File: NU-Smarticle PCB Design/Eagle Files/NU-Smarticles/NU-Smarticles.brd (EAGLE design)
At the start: 20 x 48 mm, 66 parts, among them IC1 CP2104, IC2 ATMEGA328P, Q3 DMG341, SW2 KMR2, U6 AP2112-3.3, U7 MCP73831T-2ACI/OT, U8 OPA344, U9 ADMP401, X1 JSTPH, X4 20329, Y2 CSTCE16M0V53-R0 8MHZ

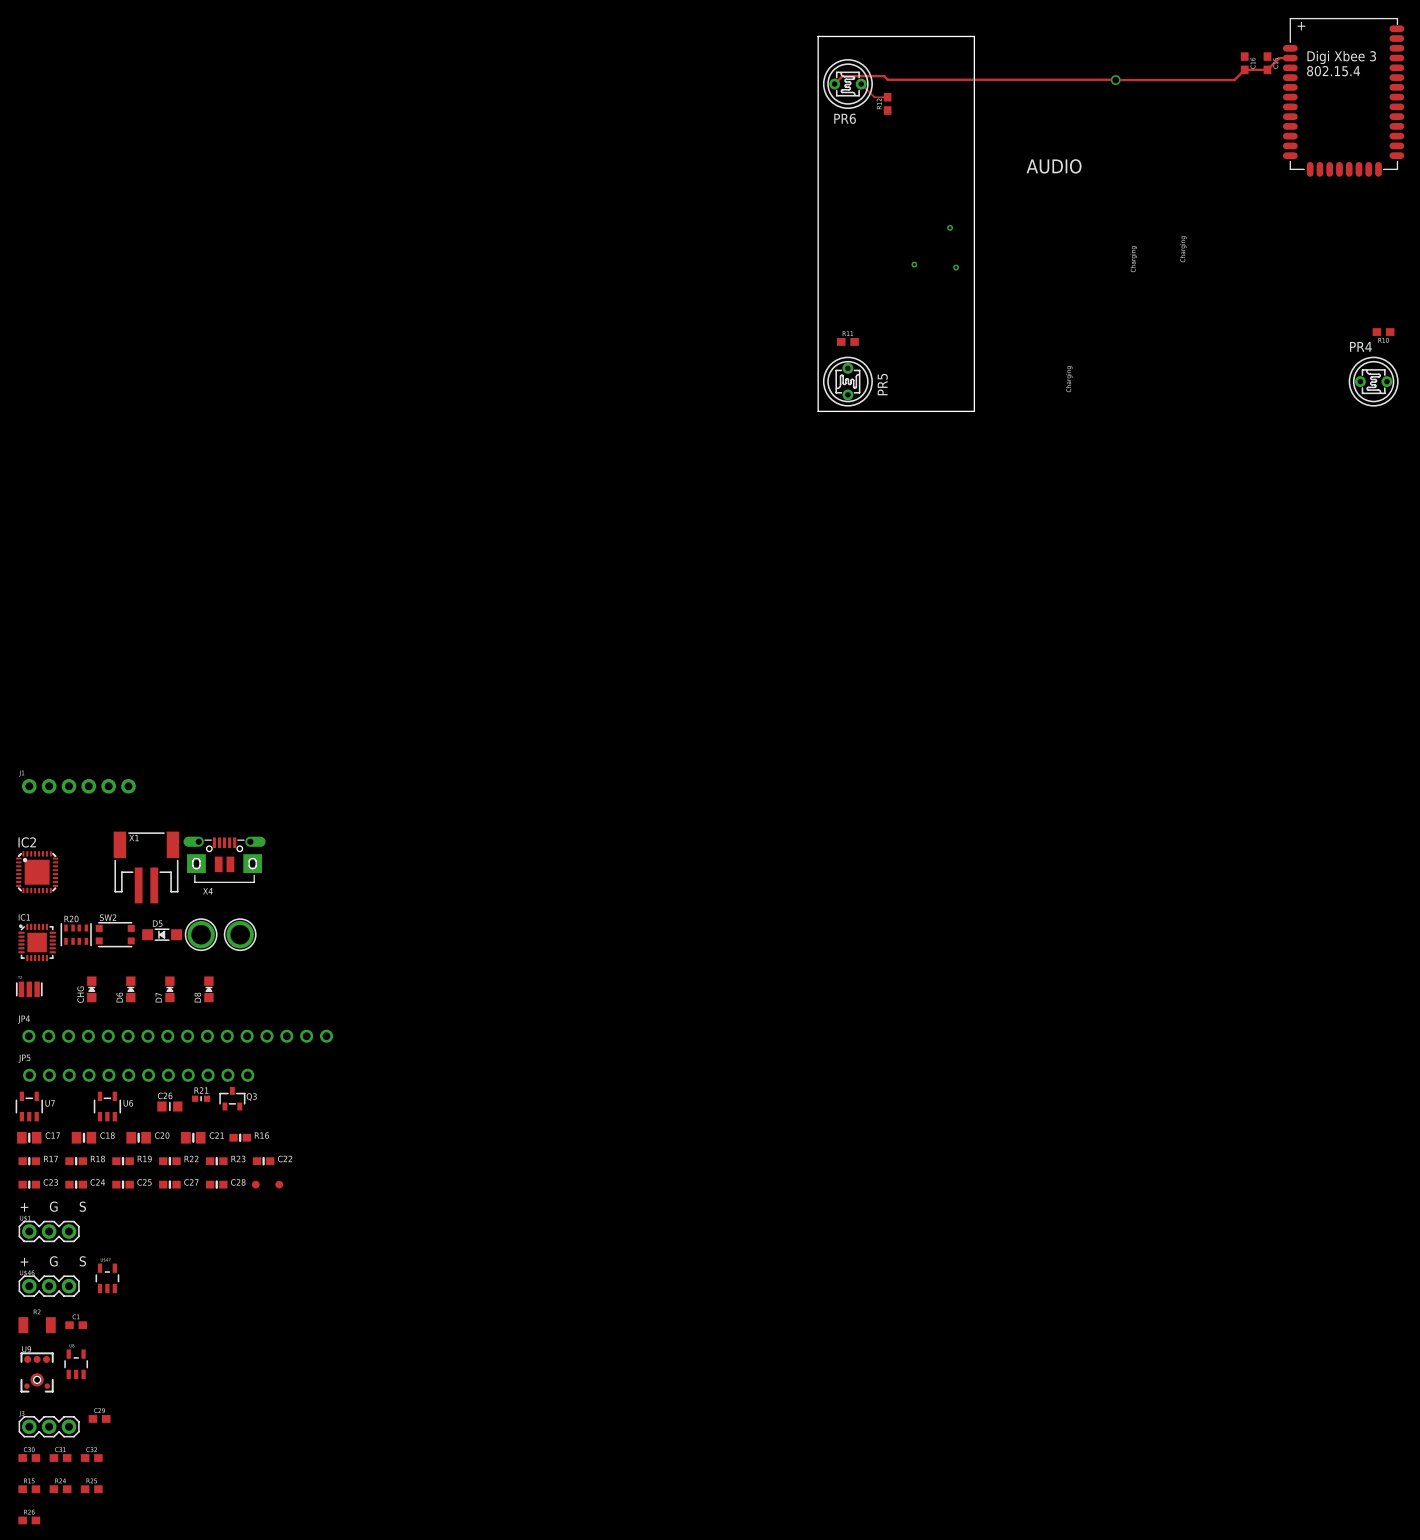
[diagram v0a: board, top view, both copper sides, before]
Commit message: include v2 Smarticles
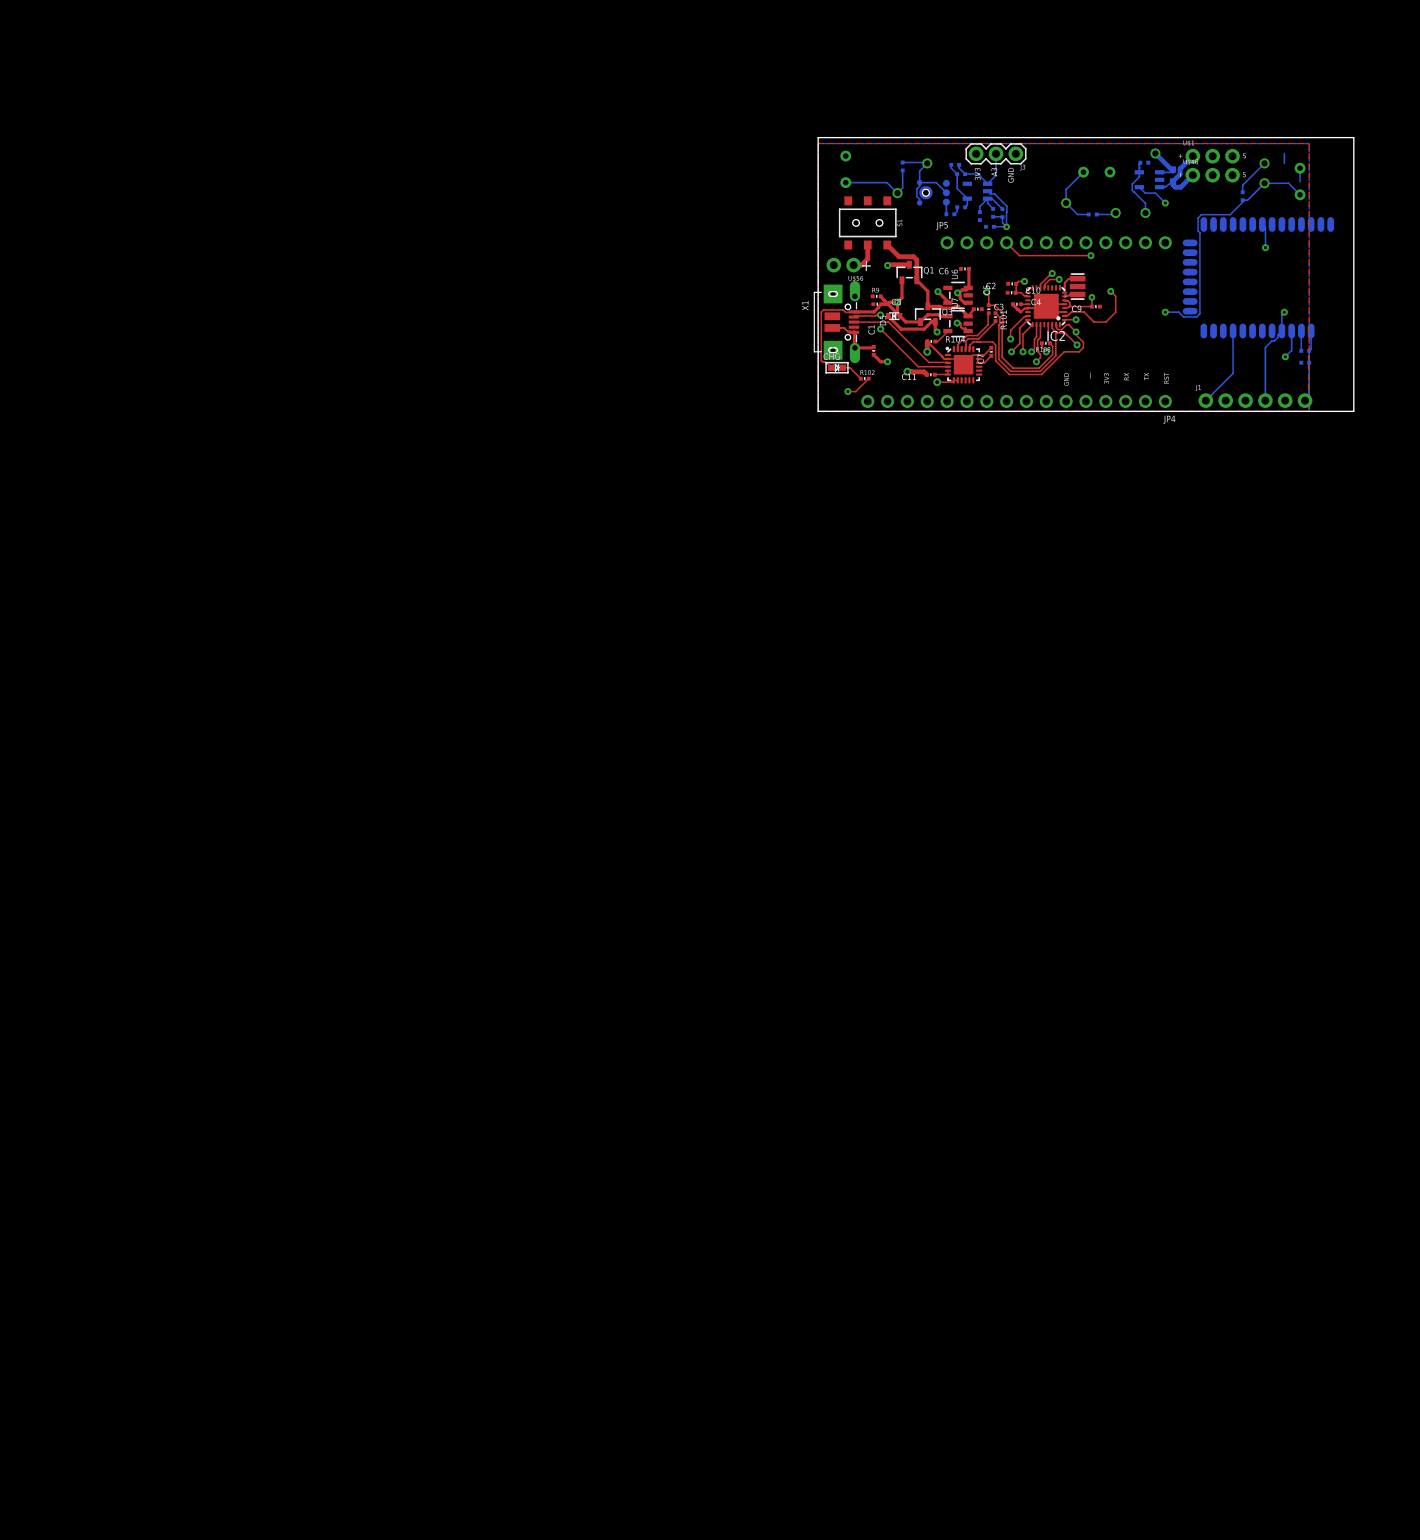
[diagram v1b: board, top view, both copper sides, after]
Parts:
- removed C20, C21: 10uF, microbuilder:0805-NO
- removed C22, C23, C24, C25: 0.1uF, microbuilder:0603-NO
- removed C26: 10uF, microbuilder:_0805MP
- removed C27, C28: 1uF, microbuilder:0603-NO
- removed C29: 100pF, SparkFun-Capacitors:0603
- removed C30: 4.7uF, SparkFun-Capacitors:0603
- removed C31: 1.0uF, SparkFun-Capacitors:0603
- removed C32: 0.1uF, SparkFun-Capacitors:0603
- removed D6: RED, microbuilder:CHIPLED_0805_NOOUTLINE
- removed D7, D8: YELLOW, microbuilder:CHIPLED_0805_NOOUTLINE
- removed FRAME1: FRAME-LETTER, SparkFun-Aesthetics:CREATIVE_COMMONS
- removed PR4, PR5, PR6: A1050_09, photo-elements:T0-46-A10XX
- removed R10, R11, R12, R15, R24: 10k, SparkFun-Resistors:0603
- removed R16, R17, R22, R23: 1K, microbuilder:0603-NO
- removed R18, R19: 10K, microbuilder:0603-NO
- removed R20: 100K, microbuilder:RESPACK_4X0603
- removed R21: 1K, microbuilder:_0603MP
- removed R25: 1.5k, SparkFun-Resistors:0603
- removed R26: 100k, SparkFun-Resistors:0603
- removed SW2: KMR2, microbuilder:BTN_KMR2_4.6X2.8
- removed U$31, U$32: MOUNTINGHOLE2.5, microbuilder:MOUNTINGHOLE_2.5_PLATED
- removed U$34, U$35: FIDUCIAL_1MM, microbuilder:FIDUCIAL_1MM
- removed X4: 20329, microbuilder:4UCONN_20329_V2
- added C10, C4, C5, C9: 0.1uF, NU-Smarticles:_0402MP
- added C11, C8: 1uF, NU-Smarticles:_0402MP
- added C12: 9.0pF, NU-Smarticles:_0402MP
- added C13: 1.0uF, NU-Smarticles:_0402MP
- added C14: 4.7uF, NU-Smarticles:_0402MP
- added C2, C7: 10uF, NU-Smarticles:_0402MP
- added C3: 10µF, microbuilder:_0402MP
- added C6: 10µF, NU-Smarticles:_0402MP
- added PH1, PH2, PH3: A1050_09, NU-Smarticles:T0-46-A10XX
- added Q1: DMG341, microbuilder:SOT23-R
- added R1: 1.5k, NU-Smarticles:_0402MP
- added R101: 1K, microbuilder:_0402MP
- added R102: 1k, NU-Smarticles:_0402MP
- added R104: 10K, microbuilder:_0402MP
- added R108, R3, R4, R6, R7, R8: 10k, NU-Smarticles:_0402MP
- added R5, R9: 100k, NU-Smarticles:_0402MP
- added S1: (no value), NU-Smarticles:SWITCH_DPDT_SMD_AYZ0202
- added U$56: LI-PO, NU-Smarticles:1X02_BATT
- C1: value 0.1uF -> 10uF; device SparkFun-Capacitors:0603 -> NU-Smarticles:_0402MP
- C15: value 9.0pF -> 1.0uF; device SparkFun-Capacitors:0603 -> NU-Smarticles:_0402MP
- C16: value 1.0uF -> 100pF; device SparkFun-Capacitors:0603 -> NU-Smarticles:_0402MP
- C17, C18: value 10µF -> 0.1uF; device microbuilder:0805-NO -> NU-Smarticles:_0402MP
- CHG: device microbuilder:CHIPLED_0805_NOOUTLINE -> microbuilder:CHIPLED_0603
- D5: device microbuilder:SOD-123 -> microbuilder:SOD-523
- IC1: value CP2104 -> CP2102N
- R2: device SparkFun-Resistors:1210 -> NU-Smarticles:_0603MP
- U6: device microbuilder:SOT23-5 -> NU-Smarticles:SOT23-5
- X1: value JSTPH -> (none); device microbuilder:JSTPH2 -> Adafruit Feather 328P:4UCONN_20329
- moved R2 206.9 mm to (45.4, 30.2), flipped to the bottom, turned to 270 degrees
- moved J3 206.2 mm to (25.3, 33.0), turned to 180 degrees
- moved U$46 206.0 mm to (48.0, 30.2)
- moved U$1 202.8 mm to (48.0, 32.7)
- moved U$47 193.9 mm to (42.4, 29.6), flipped to the bottom, turned to 270 degrees
- moved U9 189.9 mm to (13.8, 28.0), flipped to the bottom, turned to 90 degrees
- moved U8 189.4 mm to (20.4, 28.2), flipped to the bottom, turned to 270 degrees
- moved C18 184.4 mm to (41.8, 31.8), flipped to the bottom
- moved C17 169.5 mm to (22.0, 23.6), flipped to the bottom, turned to 180 degrees
- moved Y2 161.6 mm to (33.2, 16.0), turned to 90 degrees
- moved C1 161.2 mm to (7.11, 7.75), turned to 90 degrees
- moved JP5 158.6 mm to (30.5, 21.6)
- moved J1 158.5 mm to (49.6, 1.38)
- moved U7 155.5 mm to (17.9, 11.2), turned to 90 degrees
- moved U6 150.5 mm to (17.9, 14.9), turned to 90 degrees
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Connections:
- removed net N$21: IC1.3, X4.D+
- removed net N$22: IC1.4, X4.D-
- removed net N$24: D6.A, R17.2
- removed net N$25: D7.A, R23.1
- removed net N$26: D8.A, R22.1
- removed net RXLED1: D7.C, IC1.13
- removed net TXLED1: D8.C, IC1.14
- removed net VBAT: C18.1, JP5.1, Q3.3, R20.2, U7.3, X1.2
- removed net VBUS: C27.2, CHG.A, D5.A, IC1.7, IC1.8, JP5.3, Q3.1, R20.4, R22.2, R23.2, U7.4, X4.VBUS
- new net N$2: IC1.3, X1.D+
- new net N$3: IC1.4, X1.D-
- new net VCC_1: JP5.1, Q1.3, R2.1, U$47.1
- new net VIN: S1.2, U$56.1
- new net V_USB: C8.2, CHG.A, D5.A, IC1.7, IC1.8, JP5.3, Q1.1, Q3.1, R9.2, U7.4, X1.VBUS
- new net XB_DTR: J1.1, U$2.DTR/SLEEP_RQ/DIO8
- new net XB_RTS: J1.2, U$2.RTS/DIO6
- net 3.3V: now also C10.2, C12.2, C13.2, C17.1, C18.1, C2.1, C9.2, J1.5, JP4.4, PH1.1, PH2.1, PH3.1, R108.2, R3.2; no longer C15.2, C16.2, C20.1, C21.1, C24.2, C25.2, C32.1, PR4.1, PR5.1, PR6.1, R15.2, R19.2
- net A0: now also PH1.2, R6.2; no longer PR6.2, R12.2
- net A1: now also PH2.2, R7.2; no longer PR4.2, R10.2
- net A2: now also PH3.2, R8.2; no longer PR5.2, R11.2
- net A3: now also C16.2, R5.2; no longer C29.2, R26.1
- net A5: no longer JP5.11
- net A6: no longer JP4.8, R20.6, R20.7
- net A7: no longer JP4.7
- net AREF: now also C4.2; no longer C22.2, JP4.14
- net D0/RX: now also R101.1; no longer R21.1
- net D10: now also J1.4, U$2.DIN/CONFIG/DIO14
- net D11: no longer JP4.5
- net D12: no longer JP4.4
- net D13: no longer JP4.6, R17.1
- net D2: no longer JP5.6
- net D5: no longer JP5.10
- net D6: no longer JP5.9
- net D7: no longer JP4.1
- net D8: no longer U$2.DIN/CONFIG/DIO14
- net D9: now also J1.3
- net DTR: now also C5.1; no longer C23.1
- net GND: now also C10.1, C11.2, C12.1, C13.1, C15.2, C2.2, C3.2, C4.1, C6.2, C7.2, C8.1, C9.1, J1.6, JP4.6, R104.1, R4.1, R6.1, R7.1, R8.1, R9.1, U$56.2, X1.BASE@1, X1.BASE@2, X1.GND, X1.SPRT@1, X1.SPRT@2, X1.SPRT@3, X1.SPRT@4; no longer C15.1, C16.1, C20.2, C21.2, C22.1, C24.1, C25.1, C26.2, C27.1, C28.2, C31.2, C32.2, D6.C, R10.1, R11.1, R12.1, R18.1, R20.3, R20.5, R24.1, SW2.A, SW2.A', X1.1, X4.BASE@1, X4.BASE@2, X4.GND, X4.SPRT@1, X4.SPRT@2, X4.SPRT@3, X4.SPRT@4
- net N$16: now also C14.1; no longer C30.1
- net N$17: now also C16.1, R1.2, R5.1; no longer C29.1, R25.1, R26.2
- net N$18: now also R102.1; no longer R16.1
- net N$19: now also R102.2; no longer R16.2
- net N$20: now also R104.2; no longer R18.2
- net N$23: now also C6.1, D5.K; no longer C17.1, D5.C
- net N$27: now also C11.1; no longer C28.1
- net N$29: now also C14.2, R1.1; no longer C30.2, R25.2
- net N$30: now also C15.1, R3.1, R4.2; no longer C31.1, R15.1, R24.2
- net N$41: now also C7.1; no longer C26.1
- net RESET: now also C5.2, JP4.1, R108.1; no longer C23.2, R19.1, SW2.B, SW2.B'
- net RXD: now also R101.2; no longer R21.2
- net V_BATT: now also C3.1, Q1.2, Q3.3, S1.1, U7.3; no longer R2.1, U$47.1
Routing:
- net V_USB: track 0.00 -> 90.1 mm, vias 0 -> 2
- net RESET: track 0.00 -> 83.2 mm, vias 0 -> 1
- net GND: track 0.30 -> 82.6 mm, vias 0 -> 7
- net A0: track 4.08 -> 77.6 mm, vias 0 -> 3
- net A3: track 0.00 -> 58.3 mm, vias 0 -> 1
- net D9: track 0.00 -> 55.2 mm, vias 0 -> 2
- net D4: track 0.00 -> 52.1 mm, vias 0 -> 2
- net D10: track 0.00 -> 51.5 mm, vias 0 -> 2
- net A2: track 0.00 -> 51.3 mm, vias 0 -> 2
- net A1: track 0.00 -> 49.4 mm, vias 0 -> 2
- net VCC_1: track 0.00 -> 48.4 mm, vias 0 -> 2
- net D3: track 0.00 -> 46.9 mm, vias 0 -> 1
- net A4: track 0.00 -> 39.5 mm, vias 0 -> 2
- net 3.3V: track 60.1 -> 21.4 mm, vias 1 -> 5
- net TX: track 0.00 -> 38.2 mm, vias 0 -> 1
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- added copper zone on layer 16, net 3.3V
- added copper zone on layer 1, net GND
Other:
- board size 20 x 48 mm -> 68.6 x 35.1 mm
- board text added: "+"
- board text added: "3V3 A3 GND"
- board text added: "GND 3V3 DIN DOUT RTS DTR"
- board text added: "GND 3V3 DOUT DIN RTS DTR"
- board text added: "GND __ 3V3 RX TX RST"
- board text removed: "AUDIO"
- board text removed: "Charging"
